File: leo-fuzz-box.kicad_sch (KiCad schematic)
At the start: 24 parts, among them J1 IN, J2 Conn_01x04_Female, J3 OUT, J4 Power, Q1 2N3565, Q2 2N3565, SW1 Fuzz/Normal

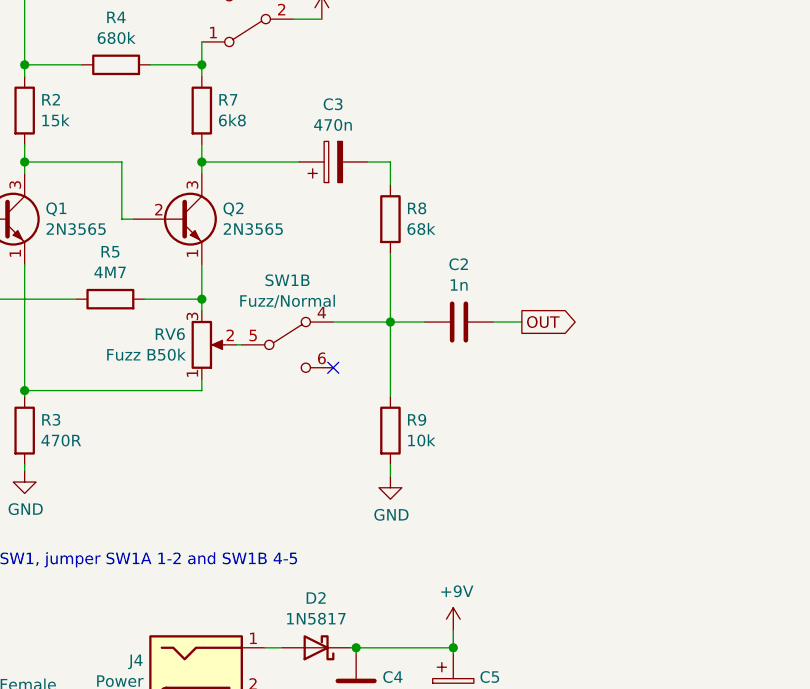
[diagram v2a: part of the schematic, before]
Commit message: v0.3: C2 goes between pot and switch
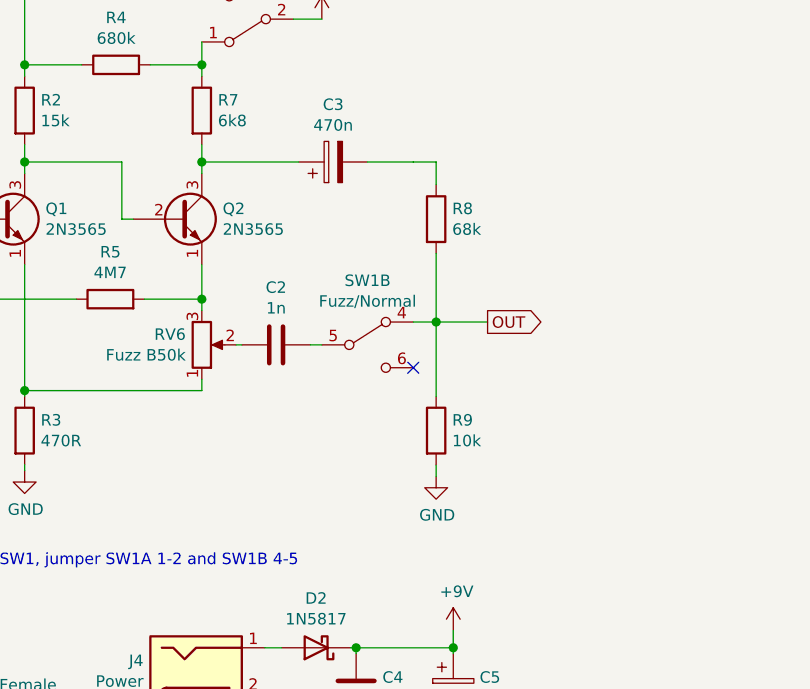
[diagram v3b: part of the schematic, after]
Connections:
- net OUT: now also R8.2, R9.1, SW1.4 (A); no longer C2.2
- net at RV6.2: now also C2.1; no longer SW1.5 (B)
- new net: C2.2, SW1.5 (B)
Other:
- moved on the sheet: C2, R8, R9, SW1B
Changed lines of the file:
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@@
-(kicad_sch (version 20200714) (host eeschema "(5.99.0-2858-ga3fc028c9)")
+(kicad_sch (version 20200820) (host eeschema "(5.99.0-2965-g3673c2369)")
   (page 1 1)
   (paper "A4")
@@
   (junction (at 76.835 59.055) (diameter 1.016) (color 0 0 0 0))
   (junction (at 93.98 97.79) (diameter 1.016) (color 0 0 0 0))
-  (junction (at 97.79 61.595) (diameter 1.016) (color 0 0 0 0))
+  (junction (at 102.87 61.595) (diameter 1.016) (color 0 0 0 0))
   (junction (at 104.775 97.79) (diameter 1.016) (color 0 0 0 0))
-  (no_connect (at 91.44 66.675))
+  (no_connect (at 100.33 66.675))
   (wire (pts (xy 21.59 99.06) (xy 36.83 99.06))
     (stroke (width 0) (type solid) (color 0 0 0 0))
@@
     (stroke (width 0) (type solid) (color 0 0 0 0))
   )
-  (wire (pts (xy 91.44 61.595) (xy 97.79 61.595))
+  (wire (pts (xy 88.9 64.135) (xy 90.17 64.135))
     (stroke (width 0) (type solid) (color 0 0 0 0))
   )
@@
     (stroke (width 0) (type solid) (color 0 0 0 0))
   )
-  (wire (pts (xy 97.79 43.815) (xy 95.25 43.815))
-    (stroke (width 0) (type solid) (color 0 0 0 0))
-  )
-  (wire (pts (xy 97.79 46.355) (xy 97.79 43.815))
-    (stroke (width 0) (type solid) (color 0 0 0 0))
-  )
-  (wire (pts (xy 97.79 53.975) (xy 97.79 61.595))
-    (stroke (width 0) (type solid) (color 0 0 0 0))
-  )
-  (wire (pts (xy 97.79 61.595) (xy 97.79 69.85))
-    (stroke (width 0) (type solid) (color 0 0 0 0))
-  )
-  (wire (pts (xy 97.79 61.595) (xy 101.6 61.595))
-    (stroke (width 0) (type solid) (color 0 0 0 0))
-  )
-  (wire (pts (xy 97.79 77.47) (xy 97.79 78.74))
+  (wire (pts (xy 100.33 43.815) (xy 95.25 43.815))
+    (stroke (width 0) (type solid) (color 0 0 0 0))
+  )
+  (wire (pts (xy 100.33 61.595) (xy 102.87 61.595))
+    (stroke (width 0) (type solid) (color 0 0 0 0))
+  )
+  (wire (pts (xy 102.87 43.815) (xy 100.33 43.815))
+    (stroke (width 0) (type solid) (color 0 0 0 0))
+  )
+  (wire (pts (xy 102.87 46.355) (xy 102.87 43.815))
+    (stroke (width 0) (type solid) (color 0 0 0 0))
+  )
+  (wire (pts (xy 102.87 53.975) (xy 102.87 61.595))
+    (stroke (width 0) (type solid) (color 0 0 0 0))
+  )
+  (wire (pts (xy 102.87 61.595) (xy 102.87 69.85))
+    (stroke (width 0) (type solid) (color 0 0 0 0))
+  )
+  (wire (pts (xy 102.87 61.595) (xy 108.585 61.595))
+    (stroke (width 0) (type solid) (color 0 0 0 0))
+  )
+  (wire (pts (xy 102.87 77.47) (xy 102.87 78.74))
     (stroke (width 0) (type solid) (color 0 0 0 0))
   )
@@
   )
   (wire (pts (xy 104.775 106.045) (xy 104.775 107.315))
-    (stroke (width 0) (type solid) (color 0 0 0 0))
-  )
-  (wire (pts (xy 109.22 61.595) (xy 112.395 61.595))
     (stroke (width 0) (type solid) (color 0 0 0 0))
   )
@@
     (effects (font (size 1.27 1.27)) (justify left))
   )
-  (global_label "OUT" (shape output) (at 112.395 61.595 0)
+  (global_label "OUT" (shape output) (at 108.585 61.595 0)
     (effects (font (size 1.27 1.27)) (justify left))
   )
@@
     )
   )
-  (symbol (lib_id "power:GND") (at 97.79 78.74 0) (unit 1)
-    (in_bom yes) (on_board yes)
-    (property "Reference" "#PWR07" (id 0) (at 97.79 85.09 0)
-      (effects (font (size 1.27 1.27)) hide)
-    )
-    (property "Value" "GND" (id 1) (at 97.9043 83.0644 0))
-    (property "Footprint" "" (id 2) (at 97.79 78.74 0)
-      (effects (font (size 1.27 1.27)) hide)
-    )
-    (property "Datasheet" "" (id 3) (at 97.79 78.74 0)
+  (symbol (lib_id "power:GND") (at 102.87 78.74 0) (unit 1)
+    (in_bom yes) (on_board yes)
+    (property "Reference" "#PWR07" (id 0) (at 102.87 85.09 0)
+      (effects (font (size 1.27 1.27)) hide)
+    )
+    (property "Value" "GND" (id 1) (at 102.9843 83.0644 0))
+    (property "Footprint" "" (id 2) (at 102.87 78.74 0)
+      (effects (font (size 1.27 1.27)) hide)
+    )
+    (property "Datasheet" "" (id 3) (at 102.87 78.74 0)
       (effects (font (size 1.27 1.27)) hide)
     )
@@
     )
   )
-  (symbol (lib_id "Device:R") (at 97.79 50.165 0) (unit 1)
-    (in_bom yes) (on_board yes)
-    (property "Reference" "R8" (id 0) (at 99.5681 49.0156 0)
-      (effects (font (size 1.27 1.27)) (justify left))
-    )
-    (property "Value" "68k" (id 1) (at 99.5681 51.3143 0)
-      (effects (font (size 1.27 1.27)) (justify left))
-    )
-    (property "Footprint" "rockola_kicad_footprints:R_DIN0207" (id 2) (at 96.012 50.165 90)
-      (effects (font (size 1.27 1.27)) hide)
-    )
-    (property "Datasheet" "~" (id 3) (at 97.79 50.165 0)
-      (effects (font (size 1.27 1.27)) hide)
-    )
-  )
-  (symbol (lib_id "Device:R") (at 97.79 73.66 0) (unit 1)
-    (in_bom yes) (on_board yes)
-    (property "Reference" "R9" (id 0) (at 99.5681 72.5106 0)
-      (effects (font (size 1.27 1.27)) (justify left))
-    )
-    (property "Value" "10k" (id 1) (at 99.5681 74.8093 0)
-      (effects (font (size 1.27 1.27)) (justify left))
-    )
-    (property "Footprint" "rockola_kicad_footprints:R_DIN0207" (id 2) (at 96.012 73.66 90)
-      (effects (font (size 1.27 1.27)) hide)
-    )
-    (property "Datasheet" "~" (id 3) (at 97.79 73.66 0)
+  (symbol (lib_id "Device:R") (at 102.87 50.165 0) (unit 1)
+    (in_bom yes) (on_board yes)
+    (property "Reference" "R8" (id 0) (at 104.6481 49.0156 0)
+      (effects (font (size 1.27 1.27)) (justify left))
+    )
+    (property "Value" "68k" (id 1) (at 104.6481 51.3143 0)
+      (effects (font (size 1.27 1.27)) (justify left))
+    )
+    (property "Footprint" "rockola_kicad_footprints:R_DIN0207" (id 2) (at 101.092 50.165 90)
+      (effects (font (size 1.27 1.27)) hide)
+    )
+    (property "Datasheet" "~" (id 3) (at 102.87 50.165 0)
+      (effects (font (size 1.27 1.27)) hide)
+    )
+  )
+  (symbol (lib_id "Device:R") (at 102.87 73.66 0) (unit 1)
+    (in_bom yes) (on_board yes)
+    (property "Reference" "R9" (id 0) (at 104.6481 72.5106 0)
+      (effects (font (size 1.27 1.27)) (justify left))
+    )
+    (property "Value" "10k" (id 1) (at 104.6481 74.8093 0)
+      (effects (font (size 1.27 1.27)) (justify left))
+    )
+    (property "Footprint" "rockola_kicad_footprints:R_DIN0207" (id 2) (at 101.092 73.66 90)
+      (effects (font (size 1.27 1.27)) hide)
+    )
+    (property "Datasheet" "~" (id 3) (at 102.87 73.66 0)
       (effects (font (size 1.27 1.27)) hide)
     )
@@
     )
   )
+  (symbol (lib_id "Device:C") (at 85.09 64.135 90) (unit 1)
+    (in_bom yes) (on_board yes)
+    (property "Reference" "C2" (id 0) (at 85.09 57.7658 90))
+    (property "Value" "1n" (id 1) (at 85.09 60.0645 90))
+    (property "Footprint" "rockola_kicad_footprints:C_Box_7.2_2.5" (id 2) (at 88.9 63.1698 0)
+      (effects (font (size 1.27 1.27)) hide)
+    )
+    (property "Datasheet" "~" (id 3) (at 85.09 64.135 0)
+      (effects (font (size 1.27 1.27)) hide)
+    )
+  )
   (symbol (lib_id "Device:CP") (at 91.44 43.815 90) (unit 1)
     (in_bom yes) (on_board yes)
@@
     )
   )
-  (symbol (lib_id "Device:C") (at 105.41 61.595 90) (unit 1)
-    (in_bom yes) (on_board yes)
-    (property "Reference" "C2" (id 0) (at 105.41 55.2258 90))
-    (property "Value" "1n" (id 1) (at 105.41 57.5245 90))
-    (property "Footprint" "rockola_kicad_footprints:C_Box_7.2_2.5" (id 2) (at 109.22 60.6298 0)
-      (effects (font (size 1.27 1.27)) hide)
-    )
-    (property "Datasheet" "~" (id 3) (at 105.41 61.595 0)
-      (effects (font (size 1.27 1.27)) hide)
-    )
-  )
   (symbol (lib_id "Device:R_POT") (at 76.835 64.135 0) (mirror x) (unit 1)
     (in_bom yes) (on_board yes)
@@
     )
   )
-  (symbol (lib_id "Switch:SW_DPDT_x2") (at 86.36 64.135 0) (unit 2)
-    (in_bom yes) (on_board yes)
-    (property "Reference" "SW1" (id 0) (at 86.36 57.004 0))
-    (property "Value" "Fuzz/Normal" (id 1) (at 86.36 59.3025 0))
-    (property "Footprint" "switches:DPDT.WIRE" (id 2) (at 86.36 64.135 0)
-      (effects (font (size 1.27 1.27)) hide)
-    )
-    (property "Datasheet" "~" (id 3) (at 86.36 64.135 0)
-      (effects (font (size 1.27 1.27)) hide)
-    )
+  (symbol (lib_id "Switch:SW_DPDT_x2") (at 95.25 64.135 0) (unit 2)
+    (in_bom yes) (on_board yes)
+    (property "Reference" "SW1" (id 0) (at 95.25 57.004 0))
+    (property "Value" "Fuzz/Normal" (id 1) (at 95.25 59.3025 0))
+    (property "Footprint" "switches:DPDT.WIRE" (id 2) (at 95.25 64.135 0)
+      (effects (font (size 1.27 1.27)) hide)
+    )
+    (property "Datasheet" "~" (id 3) (at 95.25 64.135 0)
+      (effects (font (size 1.27 1.27)) hide)
+    )
